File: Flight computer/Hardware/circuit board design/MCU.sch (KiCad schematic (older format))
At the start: 31 parts, among them J1 Conn_01x05, U11 ATSAML21J18B-AUT, U7 W74M64FV, Y3 16MHz

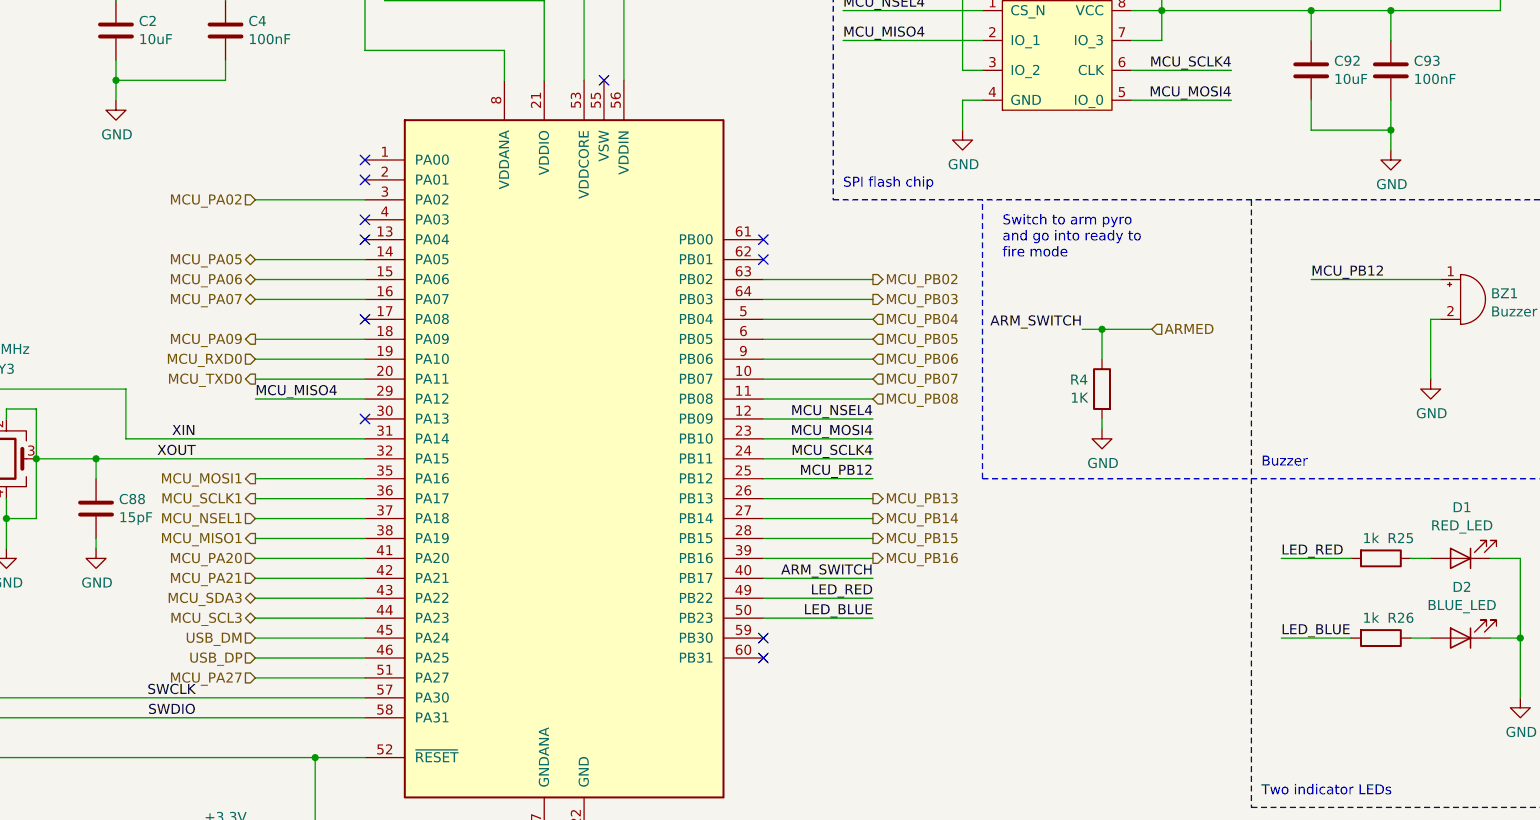
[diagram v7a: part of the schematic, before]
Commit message: changed the SERCOM ports/pins for SPI flash and radio
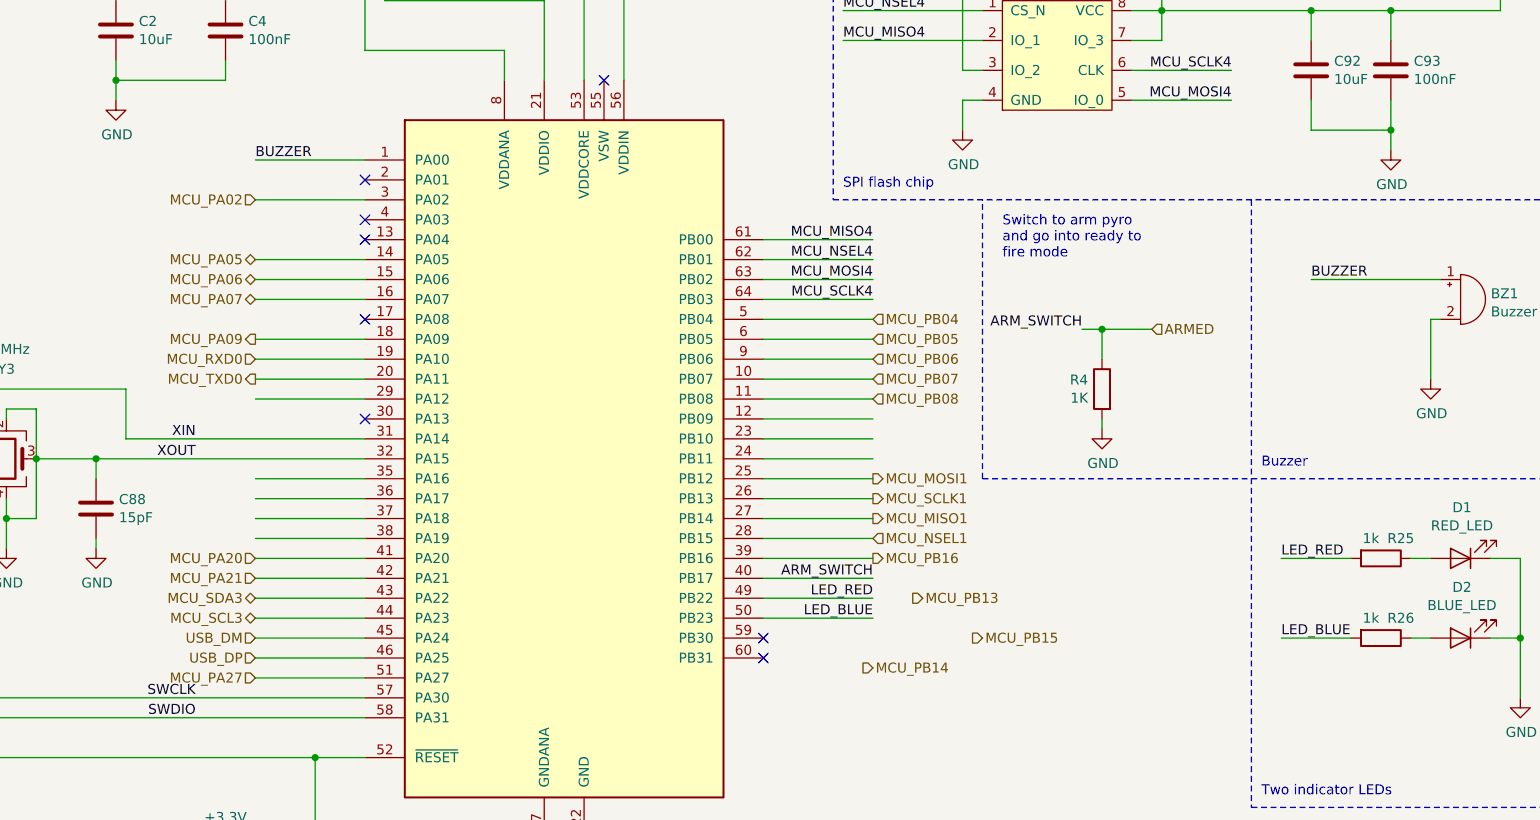
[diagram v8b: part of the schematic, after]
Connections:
- net labels added: BUZZER
- net labels removed: MCU_PB02, MCU_PB03, MCU_PB12
- wire segments 183 -> 186
- no-connect marks 11 -> 8
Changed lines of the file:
@@
 $Descr A4 11693 8268
 encoding utf-8
-Sheet 5 7
+Sheet 7 7
 Title ""
 Date "2019-09-09"
@@
 Wire Wire Line
 	9100 2300 9100 2150
-Text Label 7650 4300 2    50   ~ 0
+Text Label 7650 3500 2    50   ~ 0
 MCU_MOSI4
-Text Label 7650 4400 2    50   ~ 0
+Text Label 7650 3600 2    50   ~ 0
 MCU_SCLK4
 Text Label 9450 2450 2    50   ~ 0
@@
 Text Label 9450 2600 2    50   ~ 0
 MCU_MOSI4
-Text HLabel 7650 3500 2    50   Output ~ 0
-MCU_PB02
 Text HLabel 7650 4100 2    50   Input ~ 0
 MCU_PB08
-Text Label 4550 4100 0    50   ~ 0
-MCU_MISO4
 $Comp
 L power:GND #PWR021
@@
 Wire Wire Line
 	5100 4500 4550 4500
-NoConn ~ 7100 5400
 Wire Notes Line
 	7450 1500 7450 3100
@@
 Text Notes 7500 3050 0    50   ~ 0
 SPI flash chip
-Text HLabel 7650 3600 2    50   Output ~ 0
-MCU_PB03
 Wire Wire Line
 	7100 3600 7650 3600
-Text Label 7650 4200 2    50   ~ 0
+Text Label 7650 3400 2    50   ~ 0
 MCU_NSEL4
 Wire Wire Line
@@
 	7650 4500 7100 4500
 Text Label 9850 3500 0    50   ~ 0
-MCU_PB12
+BUZZER
 Wire Wire Line
 	9850 3500 10500 3500
@@
 Wire Wire Line
 	7100 4700 7650 4700
-Text HLabel 7650 4600 2    50   Output ~ 0
+Text HLabel 7850 5100 2    50   Output ~ 0
 MCU_PB13
-Text HLabel 7650 4700 2    50   Output ~ 0
+Text HLabel 7600 5450 2    50   Output ~ 0
 MCU_PB14
 Wire Wire Line
@@
 Wire Wire Line
 	7100 4900 7650 4900
-Text HLabel 7650 4800 2    50   Output ~ 0
+Text HLabel 8150 5300 2    50   Output ~ 0
 MCU_PB15
 Text HLabel 7650 4900 2    50   Output ~ 0
@@
 	1    0    0    -1
 $EndComp
-NoConn ~ 7100 3400
-NoConn ~ 7100 3300
 Text HLabel 4550 5400 0    50   Input ~ 0
 USB_DP
@@
 Two indicator LEDs
 NoConn ~ 5100 3000
-NoConn ~ 5100 2900
 Wire Wire Line
 	1000 1150 900  1150
@@
 $EndComp
 NoConn ~ 7100 5300
-Text Label 7650 4500 2    50   ~ 0
-MCU_PB12
-Text HLabel 4550 4800 0    50   Output ~ 0
+Text HLabel 7650 4700 2    50   Output ~ 0
 MCU_MISO1
-Text HLabel 4550 4700 0    50   Input ~ 0
+Text HLabel 7650 4800 2    50   Input ~ 0
 MCU_NSEL1
-Text HLabel 4550 4600 0    50   Output ~ 0
+Text HLabel 7650 4600 2    50   Output ~ 0
 MCU_SCLK1
-Text HLabel 4550 4500 0    50   Output ~ 0
+Text HLabel 7650 4500 2    50   Output ~ 0
 MCU_MOSI1
 Wire Wire Line
@@
 	3300 4700 3300 4850
 Connection ~ 3300 4700
+Text Label 7650 3300 2    50   ~ 0
+MCU_MISO4
+NoConn ~ 7100 5400
+Text Label 4550 2900 0    50   ~ 0
+BUZZER
+Wire Wire Line
+	7100 3300 7650 3300
+Wire Wire Line
+	7100 3400 7650 3400
+Wire Wire Line
+	4550 2900 5100 2900
 $EndSCHEMATC
